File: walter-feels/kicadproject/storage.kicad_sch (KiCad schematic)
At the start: 4 parts, among them J1 693072010801, U13 CM1624-08DE

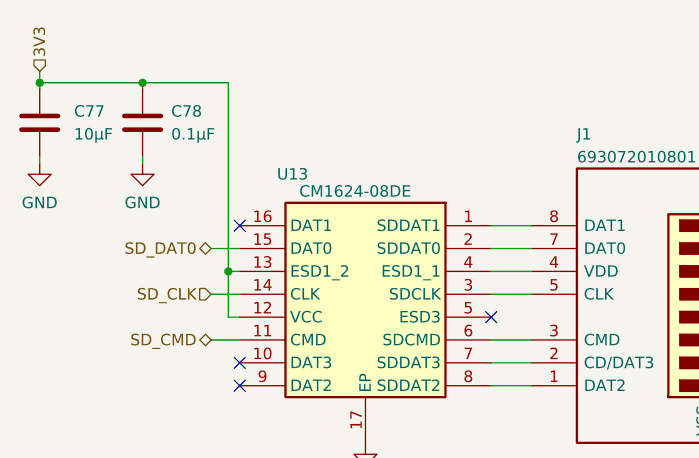
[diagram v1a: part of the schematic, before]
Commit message: Updated Walter Feels to V2.3
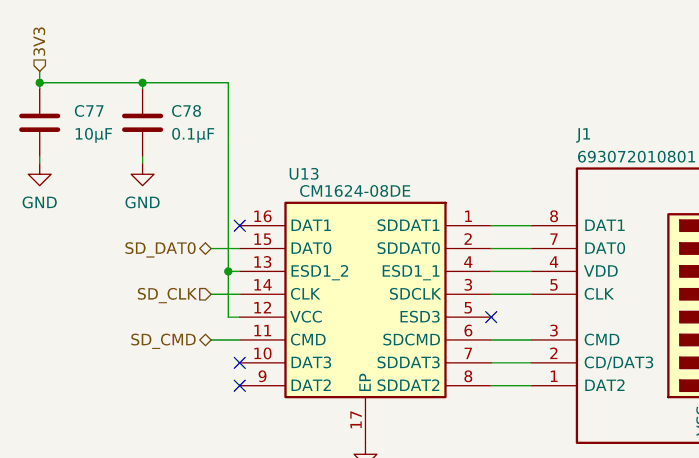
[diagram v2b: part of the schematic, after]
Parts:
- J1: JLCPCB C9900019763 -> C5912397
- U13: JLCPCB (none) -> C605363
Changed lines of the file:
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@@
   (title_block
     (title "Walter Feels")
-    (date "2023-10-13")
-    (rev "2.1")
+    (date "2024-03-13")
+    (rev "2.3")
     (company "DPTechnics BV")
     (comment 1 "Checked by: Jonas Maes")
@@
       (effects (font (size 1.27 1.27)) (justify left) hide)
     )
-    (property "JLCPCB" "C9900019763" (id 4) (at 207.645 90.805 0)
+    (property "JLCPCB" "C5912397" (id 4) (at 207.645 90.805 0)
       (effects (font (size 1.27 1.27)) hide)
     )
@@
   (symbol (lib_id "CM1624-08DE:CM1624-08DE") (at 127 88.265 0) (mirror y) (unit 1)
     (in_bom yes) (on_board yes)
-    (property "Reference" "U13" (id 0) (at 120.65 81.28 0)
+    (property "Reference" "U13" (id 0) (at 121.92 81.28 0)
       (effects (font (size 1.27 1.27)) (justify left))
     )
@@
       (effects (font (size 1.27 1.27)) hide)
     )
+    (property "JLCPCB" "C605363" (id 4) (at 127 88.265 0)
+      (effects (font (size 1.27 1.27)) hide)
+    )

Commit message: Updated to version 2.4
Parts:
- C77: value 10µF -> 4.7μF; footprint Capacitor_SMD:C_1206_3216Metric -> Capacitor_SMD:C_0603_1608Metric; JLCPCB C13585 -> C19666
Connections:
- net 3V3: now also C77.2; no longer C77.1
- net GND: now also C77.1; no longer C77.2
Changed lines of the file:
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@@
   (title_block
     (title "Walter Feels")
-    (date "2024-03-13")
-    (rev "2.3")
+    (date "2025-02-12")
+    (rev "2.4")
     (company "DPTechnics BV")
     (comment 1 "Checked by: Jonas Maes")
@@
     (pin "2")
   )
+  (symbol (lib_id "Device:C") (at 90.805 75.565 180) (unit 1)
+    (in_bom yes) (on_board yes)
+    (property "Reference" "C77" (id 0) (at 93.345 74.295 0)
+      (effects (font (size 1.27 1.27)) (justify right))
+    )
+    (property "Value" "4.7μF" (id 1) (at 93.345 76.835 0)
+      (effects (font (size 1.27 1.27)) (justify right))
+    )
+    (property "Footprint" "Capacitor_SMD:C_0603_1608Metric" (id 2) (at 89.8398 71.755 0)
+      (effects (font (size 1.27 1.27)) hide)
+    )
+    (property "Datasheet" "~" (id 3) (at 90.805 75.565 0)
+      (effects (font (size 1.27 1.27)) hide)
+    )
+    (property "JLCPCB" "C19666" (id 4) (at 90.805 75.565 0)
+      (effects (font (size 1.27 1.27)) hide)
+    )
+    (property "PAGE" "" (id 5) (at 90.805 75.565 0)
+      (effects (font (size 1.27 1.27)) hide)
+    )
+    (pin "1")
+    (pin "2")
+  )
   (symbol (lib_id "power:GND") (at 90.805 80.01 0) (unit 1)
     (in_bom yes) (on_board yes) (fields_autoplaced)
@@
     (pin "1")
   )
-  (symbol (lib_id "Device:C") (at 90.805 75.565 0) (unit 1)
-    (in_bom yes) (on_board yes) (fields_autoplaced)
-    (property "Reference" "C77" (id 0) (at 94.615 74.2949 0)
-      (effects (font (size 1.27 1.27)) (justify left))
-    )
-    (property "Value" "10µF" (id 1) (at 94.615 76.8349 0)
-      (effects (font (size 1.27 1.27)) (justify left))
-    )
-    (property "Footprint" "Capacitor_SMD:C_1206_3216Metric" (id 2) (at 91.7702 79.375 0)
-      (effects (font (size 1.27 1.27)) hide)
-    )
-    (property "Datasheet" "~" (id 3) (at 90.805 75.565 0)
-      (effects (font (size 1.27 1.27)) hide)
-    )
-    (property "JLCPCB" "C13585" (id 4) (at 90.805 75.565 0)
-      (effects (font (size 1.27 1.27)) hide)
-    )
-    (property "PAGE" "" (id 5) (at 90.805 75.565 0)
-      (effects (font (size 1.27 1.27)) hide)
-    )
-    (pin "1")
-    (pin "2")
-  )
   (symbol (lib_id "CM1624-08DE:CM1624-08DE") (at 127 88.265 0) (mirror y) (unit 1)

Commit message: Updated Walter Feels project to version 2.6
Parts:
- removed U13: CM1624-08DE, LIB_CM1624-08DE:SON40P135X330X55-17N, symbol CM1624-08DE:CM1624-08DE
- added D6: D3V3X4U10LP-7, D3V3X4U10LP-7:D3V3X4U10LP7, symbol D3V3X4U10LP-7:D3V3X4U10LP-7
- added R26, R29, R30, R31, R32, R33: 10kΩ, Resistor_SMD:R_0603_1608Metric, symbol Device:R
- C77: value 4.7μF -> 1μF; JLCPCB C19666 -> C15849
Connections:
- net 3V3: now also J1.4 (VDD), D6.4 (IO3), D6.7 (NC), R26.1, R29.1, R30.1, R31.1, R32.1, R33.1
- net GND: now also D6.3 (VSS), D6.8 (VSS)
- net SD_CLK: now also J1.5 (CLK), D6.2 (IO2), D6.9 (NC), R31.2
- net SD_CMD: now also J1.3 (CMD), D6.5 (IO4), D6.6 (NC), R30.2
- net SD_DAT0: now also J1.7 (DAT0), D6.1 (IO1), D6.10 (NC), R32.2
- net at J1.1 (DAT2): now also R26.2
- net at J1.2 (CD/DAT3): now also R29.2
- net at J1.8 (DAT1): now also R33.2
- no-connect marks 4 -> 0
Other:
- moved on the sheet: C78, J1
